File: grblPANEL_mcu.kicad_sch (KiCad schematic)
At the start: 31 parts, among them J201 2x5x1.27mm, J202 USB_C_Receptacle_USB2.0, SW201 SW_Push, SW202 SW_Push, U201 STM32G0B1CxTxN, U202 USBLC6-2SC6, Y201 8MHz

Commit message: PCB layout - WIP
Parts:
- SW201, SW202: footprint Connector_Pin:Pin_D1.0mm_L10.0mm_LooseFit -> Button_Switch_SMD:SW_Push_1P1T_NO_6x6mm_H9.5mm
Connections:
- net GND: no longer C204.2
- net VDDIO2: now reaches C204.1, R204.1, U201.31 (VDDIO2)
- net CONN_SWDIO: now reaches D203.1 (A1), J201.2 (Pin_2), R209.1
- net LED: now reaches R205.1, U201.19 (PB0)
- net VSS2: now reaches R203.1, U201.30 (VSS)
- net VSS2: now also C204.2
- net VREF+: now reaches R201.2, U201.5 (VREF+)
- net LED_K: now reaches D201.1 (K), R205.2
- net CONN_SWCLK: now reaches D204.1 (A1), J201.4 (Pin_4), R210.1
- net CONN_~{RST}: now reaches D205.1 (A1), J201.10 (Pin_10), R211.1
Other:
- moved on the sheet: R201
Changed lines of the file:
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@@
     (stroke (width 0) (type default) (color 0 0 0 0))
   )
-  (wire (pts (xy 74.93 60.96) (xy 78.74 60.96))
+  (wire (pts (xy 69.85 60.96) (xy 78.74 60.96))
     (stroke (width 0) (type default) (color 0 0 0 0))
   )
@@
     (stroke (width 0) (type default) (color 0 0 0 0))
   )
-  (wire (pts (xy 114.3 49.53) (xy 114.3 50.8))
+  (wire (pts (xy 114.3 49.53) (xy 114.3 53.34))
     (stroke (width 0) (type default) (color 0 0 0 0))
   )
@@
     (stroke (width 0) (type default) (color 0 0 0 0))
   )
-  (wire (pts (xy 59.69 62.23) (xy 59.69 60.96))
+  (wire (pts (xy 54.61 62.23) (xy 54.61 60.96))
     (stroke (width 0) (type default) (color 0 0 0 0))
   )
@@
     (stroke (width 0) (type default) (color 0 0 0 0))
   )
+  (wire (pts (xy 114.3 53.34) (xy 120.65 53.34))
+    (stroke (width 0) (type default) (color 0 0 0 0))
+  )
   (wire (pts (xy 58.42 76.2) (xy 78.74 76.2))
     (stroke (width 0) (type default) (color 0 0 0 0))
@@
     (stroke (width 0) (type default) (color 0 0 0 0))
   )
-  (wire (pts (xy 59.69 60.96) (xy 67.31 60.96))
+  (wire (pts (xy 54.61 60.96) (xy 62.23 60.96))
     (stroke (width 0) (type default) (color 0 0 0 0))
   )
@@
     (effects (font (size 1.27 1.27)) (justify left bottom))
   )
+  (label "CONN_SWDIO" (at 229.87 36.83 0)
+    (effects (font (size 1.27 1.27)) (justify left bottom))
+  )
   (label "SWCLK{slash}BOOT0" (at 63.5 104.14 0)
     (effects (font (size 1.27 1.27)) (justify left bottom))
@@
     (effects (font (size 1.27 1.27)) (justify right bottom))
   )
+  (label "CONN_~{RST}" (at 229.87 46.99 0)
+    (effects (font (size 1.27 1.27)) (justify left bottom))
+  )
   (label "XTAL_IN" (at 139.7 132.08 0)
     (effects (font (size 1.27 1.27)) (justify left bottom))
@@
     (effects (font (size 1.27 1.27)) (justify left bottom))
   )
+  (label "VSS2" (at 120.65 53.34 180)
+    (effects (font (size 1.27 1.27)) (justify right bottom))
+  )
   (label "USB_CONN_CC1" (at 224.79 91.44 0)
+    (effects (font (size 1.27 1.27)) (justify left bottom))
+  )
+  (label "VDDIO2" (at 100.33 44.45 0)
     (effects (font (size 1.27 1.27)) (justify left bottom))
   )
@@
     (effects (font (size 1.27 1.27)) (justify right bottom))
   )
+  (label "VSS2" (at 99.06 134.62 0)
+    (effects (font (size 1.27 1.27)) (justify left bottom))
+  )
   (label "~{RST}" (at 273.05 46.99 180)
     (effects (font (size 1.27 1.27)) (justify right bottom))
@@
     (effects (font (size 1.27 1.27)) (justify right bottom))
   )
+  (label "CONN_SWCLK" (at 229.87 39.37 0)
+    (effects (font (size 1.27 1.27)) (justify left bottom))
+  )
   (label "USB_D-" (at 198.12 139.7 0)
     (effects (font (size 1.27 1.27)) (justify left bottom))
   )
   (label "USB_D+" (at 63.5 99.06 0)
+    (effects (font (size 1.27 1.27)) (justify left bottom))
+  )
+  (label "LED_K" (at 129.54 60.96 0)
+    (effects (font (size 1.27 1.27)) (justify left bottom))
+  )
+  (label "VREF+" (at 78.74 60.96 180)
+    (effects (font (size 1.27 1.27)) (justify right bottom))
+  )
+  (label "LED" (at 118.11 60.96 0)
     (effects (font (size 1.27 1.27)) (justify left bottom))
   )
@@
       (effects (font (size 1.27 1.27)) hide)
     )
-    (property "Footprint" "Connector_Pin:Pin_D1.0mm_L10.0mm_LooseFit" (id 2) (at 123.19 171.45 0)
+    (property "Footprint" "Button_Switch_SMD:SW_Push_1P1T_NO_6x6mm_H9.5mm" (id 2) (at 123.19 171.45 0)
       (effects (font (size 1.27 1.27)) hide)
     )
@@
     (pin "1")
   )
-  (symbol (lib_id "power:GND") (at 59.69 62.23 0) (unit 1)
-    (in_bom yes) (on_board yes)
-    (property "Reference" "#PWR0203" (id 0) (at 59.69 68.58 0)
-      (effects (font (size 1.27 1.27)) hide)
-    )
-    (property "Value" "GND" (id 1) (at 62.23 64.77 0)
-      (effects (font (size 1.27 1.27)) hide)
-    )
-    (property "Footprint" "" (id 2) (at 59.69 62.23 0)
-      (effects (font (size 1.27 1.27)) hide)
-    )
-    (property "Datasheet" "" (id 3) (at 59.69 62.23 0)
+  (symbol (lib_id "power:GND") (at 54.61 62.23 0) (unit 1)
+    (in_bom yes) (on_board yes)
+    (property "Reference" "#PWR0203" (id 0) (at 54.61 68.58 0)
+      (effects (font (size 1.27 1.27)) hide)
+    )
+    (property "Value" "GND" (id 1) (at 57.15 64.77 0)
+      (effects (font (size 1.27 1.27)) hide)
+    )
+    (property "Footprint" "" (id 2) (at 54.61 62.23 0)
+      (effects (font (size 1.27 1.27)) hide)
+    )
+    (property "Datasheet" "" (id 3) (at 54.61 62.23 0)
       (effects (font (size 1.27 1.27)) hide)
     )
@@
     (pin "1")
     (pin "2")
-  )
-  (symbol (lib_id "power:GND") (at 114.3 50.8 0) (unit 1)
-    (in_bom yes) (on_board yes)
-    (property "Reference" "#PWR0206" (id 0) (at 114.3 57.15 0)
-      (effects (font (size 1.27 1.27)) hide)
-    )
-    (property "Value" "GND" (id 1) (at 118.11 53.34 0)
-      (effects (font (size 1.27 1.27)) hide)
-    )
-    (property "Footprint" "" (id 2) (at 114.3 50.8 0)
-      (effects (font (size 1.27 1.27)) hide)
-    )
-    (property "Datasheet" "" (id 3) (at 114.3 50.8 0)
-      (effects (font (size 1.27 1.27)) hide)
-    )
-    (pin "1")
   )
   (symbol (lib_id "Device:R") (at 212.09 101.6 0) (unit 1)
@@
     (pin "2")
   )
-  (symbol (lib_id "Device:R") (at 71.12 60.96 90) (unit 1)
-    (in_bom yes) (on_board yes)
-    (property "Reference" "R201" (id 0) (at 71.12 58.42 90))
-    (property "Value" "0" (id 1) (at 71.12 63.5 90))
-    (property "Footprint" "Resistor_SMD:R_0603_1608Metric" (id 2) (at 71.12 62.738 90)
-      (effects (font (size 1.27 1.27)) hide)
-    )
-    (property "Datasheet" "~" (id 3) (at 71.12 60.96 0)
+  (symbol (lib_id "Device:R") (at 66.04 60.96 90) (unit 1)
+    (in_bom yes) (on_board yes)
+    (property "Reference" "R201" (id 0) (at 66.04 58.42 90))
+    (property "Value" "0" (id 1) (at 66.04 63.5 90))
+    (property "Footprint" "Resistor_SMD:R_0603_1608Metric" (id 2) (at 66.04 62.738 90)
+      (effects (font (size 1.27 1.27)) hide)
+    )
+    (property "Datasheet" "~" (id 3) (at 66.04 60.96 0)
       (effects (font (size 1.27 1.27)) hide)
     )
@@
       (effects (font (size 1.27 1.27)) hide)
     )
-    (property "Footprint" "Connector_Pin:Pin_D1.0mm_L10.0mm_LooseFit" (id 2) (at 63.5 176.53 0)
-      (effects (font (size 1.27 1.27)) hide)
-    )
+    (property "Footprint" "Button_Switch_SMD:SW_Push_1P1T_NO_6x6mm_H9.5mm" (id 2) (at 63.5 176.53 0)
+      (effects (font (size 1.27 1.27)) hide)
+    )

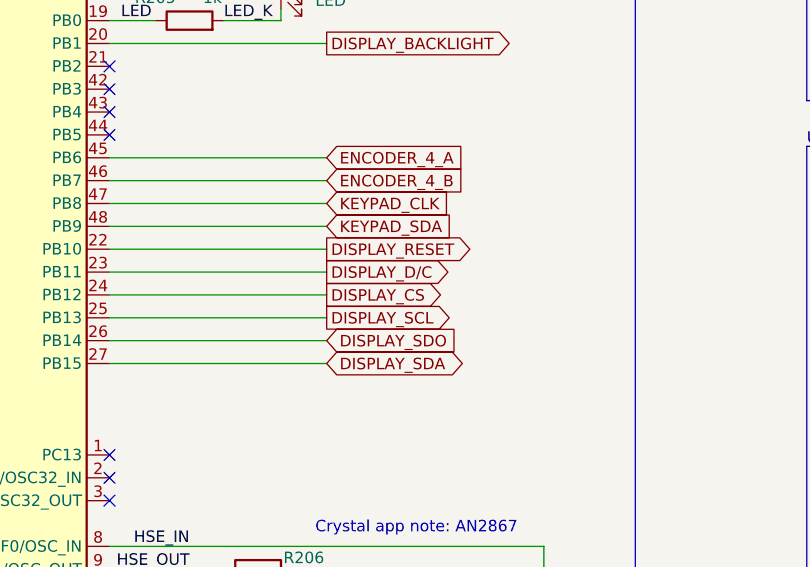
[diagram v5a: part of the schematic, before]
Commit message: 1st crack at display routing
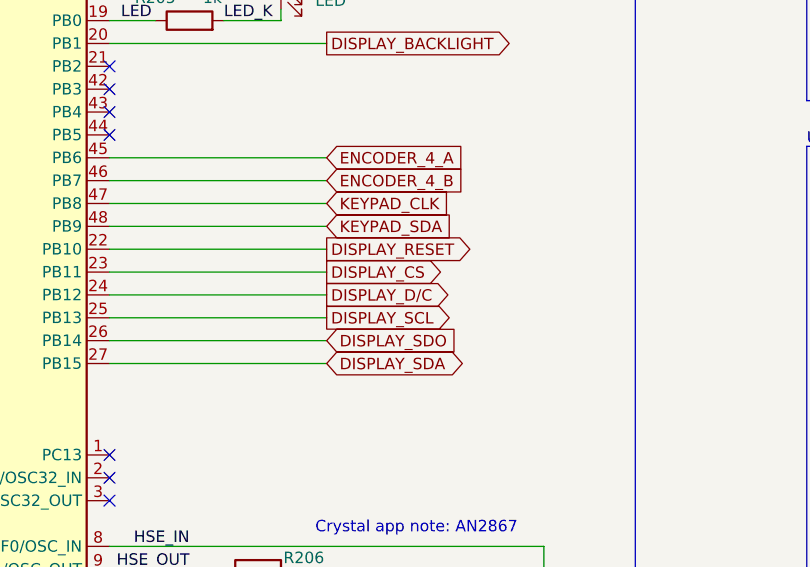
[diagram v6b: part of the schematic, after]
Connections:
- net DISPLAY_CS: now also U201.23 (PB11); no longer U201.24 (PB12)
- net DISPLAY_D/C: now also U201.24 (PB12); no longer U201.23 (PB11)
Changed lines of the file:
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@@
     )
   )
-  (global_label "DISPLAY_D{slash}C" (shape output) (at 140.97 88.9 0) (fields_autoplaced)
+  (global_label "DISPLAY_D{slash}C" (shape output) (at 140.97 91.44 0) (fields_autoplaced)
     (effects (font (size 1.27 1.27)) (justify left))
-    (property "Intersheet References" "${INTERSHEET_REFS}" (id 0) (at 155.7807 88.8206 0)
+    (property "Intersheet References" "${INTERSHEET_REFS}" (id 0) (at 155.7807 91.3606 0)
       (effects (font (size 1.27 1.27)) (justify left) hide)
     )
@@
     )
   )
-  (global_label "DISPLAY_CS" (shape output) (at 140.97 91.44 0) (fields_autoplaced)
+  (global_label "DISPLAY_CS" (shape output) (at 140.97 88.9 0) (fields_autoplaced)
     (effects (font (size 1.27 1.27)) (justify left))
-    (property "Intersheet References" "${INTERSHEET_REFS}" (id 0) (at 154.3898 91.3606 0)
+    (property "Intersheet References" "${INTERSHEET_REFS}" (id 0) (at 154.3898 88.8206 0)
       (effects (font (size 1.27 1.27)) (justify left) hide)
     )

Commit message: reset & bootloader buttons
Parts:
- SW201, SW202: footprint Button_Switch_SMD:SW_Push_1P1T_NO_6x6mm_H9.5mm -> Button_Switch_SMD:SW_SPST_PTS810
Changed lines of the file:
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@@
       (effects (font (size 1.27 1.27)) hide)
     )
-    (property "Footprint" "Button_Switch_SMD:SW_Push_1P1T_NO_6x6mm_H9.5mm" (id 2) (at 123.19 171.45 0)
+    (property "Footprint" "Button_Switch_SMD:SW_SPST_PTS810" (id 2) (at 123.19 171.45 0)
       (effects (font (size 1.27 1.27)) hide)
     )
@@
       (effects (font (size 1.27 1.27)) hide)
     )
-    (property "Footprint" "Button_Switch_SMD:SW_Push_1P1T_NO_6x6mm_H9.5mm" (id 2) (at 63.5 176.53 0)
-      (effects (font (size 1.27 1.27)) hide)
-    )
+    (property "Footprint" "Button_Switch_SMD:SW_SPST_PTS810" (id 2) (at 63.5 176.53 0)
+      (effects (font (size 1.27 1.27)) hide)
+    )

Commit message: more routing
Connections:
- net ENCODER_2_A: now also U201.45 (PB6); no longer U201.11 (PA0)
- net ENCODER_2_B: now also U201.46 (PB7); no longer U201.12 (PA1)
- net ENCODER_4_A: now also U201.11 (PA0); no longer U201.45 (PB6)
- net ENCODER_4_B: now also U201.12 (PA1); no longer U201.46 (PB7)
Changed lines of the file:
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@@
     )
   )
-  (global_label "ENCODER_4_A" (shape input) (at 140.97 76.2 0) (fields_autoplaced)
+  (global_label "ENCODER_2_A" (shape input) (at 140.97 76.2 0) (fields_autoplaced)
     (effects (font (size 1.27 1.27)) (justify left))
     (property "Intersheet References" "${INTERSHEET_REFS}" (id 0) (at 156.3855 76.1206 0)
@@
     )
   )
-  (global_label "ENCODER_2_B" (shape input) (at 58.42 71.12 180) (fields_autoplaced)
+  (global_label "ENCODER_4_B" (shape input) (at 58.42 71.12 180) (fields_autoplaced)
     (effects (font (size 1.27 1.27)) (justify right))
     (property "Intersheet References" "${INTERSHEET_REFS}" (id 0) (at 42.8231 71.0406 0)
@@
     )
   )
-  (global_label "ENCODER_2_A" (shape input) (at 58.42 68.58 180) (fields_autoplaced)
+  (global_label "ENCODER_4_A" (shape input) (at 58.42 68.58 180) (fields_autoplaced)
     (effects (font (size 1.27 1.27)) (justify right))
     (property "Intersheet References" "${INTERSHEET_REFS}" (id 0) (at 43.0045 68.5006 0)
@@
     )
   )
-  (global_label "ENCODER_4_B" (shape input) (at 140.97 78.74 0) (fields_autoplaced)
+  (global_label "ENCODER_2_B" (shape input) (at 140.97 78.74 0) (fields_autoplaced)
     (effects (font (size 1.27 1.27)) (justify left))
     (property "Intersheet References" "${INTERSHEET_REFS}" (id 0) (at 156.5669 78.6606 0)
